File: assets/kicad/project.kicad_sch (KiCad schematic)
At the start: 22 parts, among them J1 Adafruit microSD, J2 EPD, J3 RTC, J4 Screw_Terminal_01x03

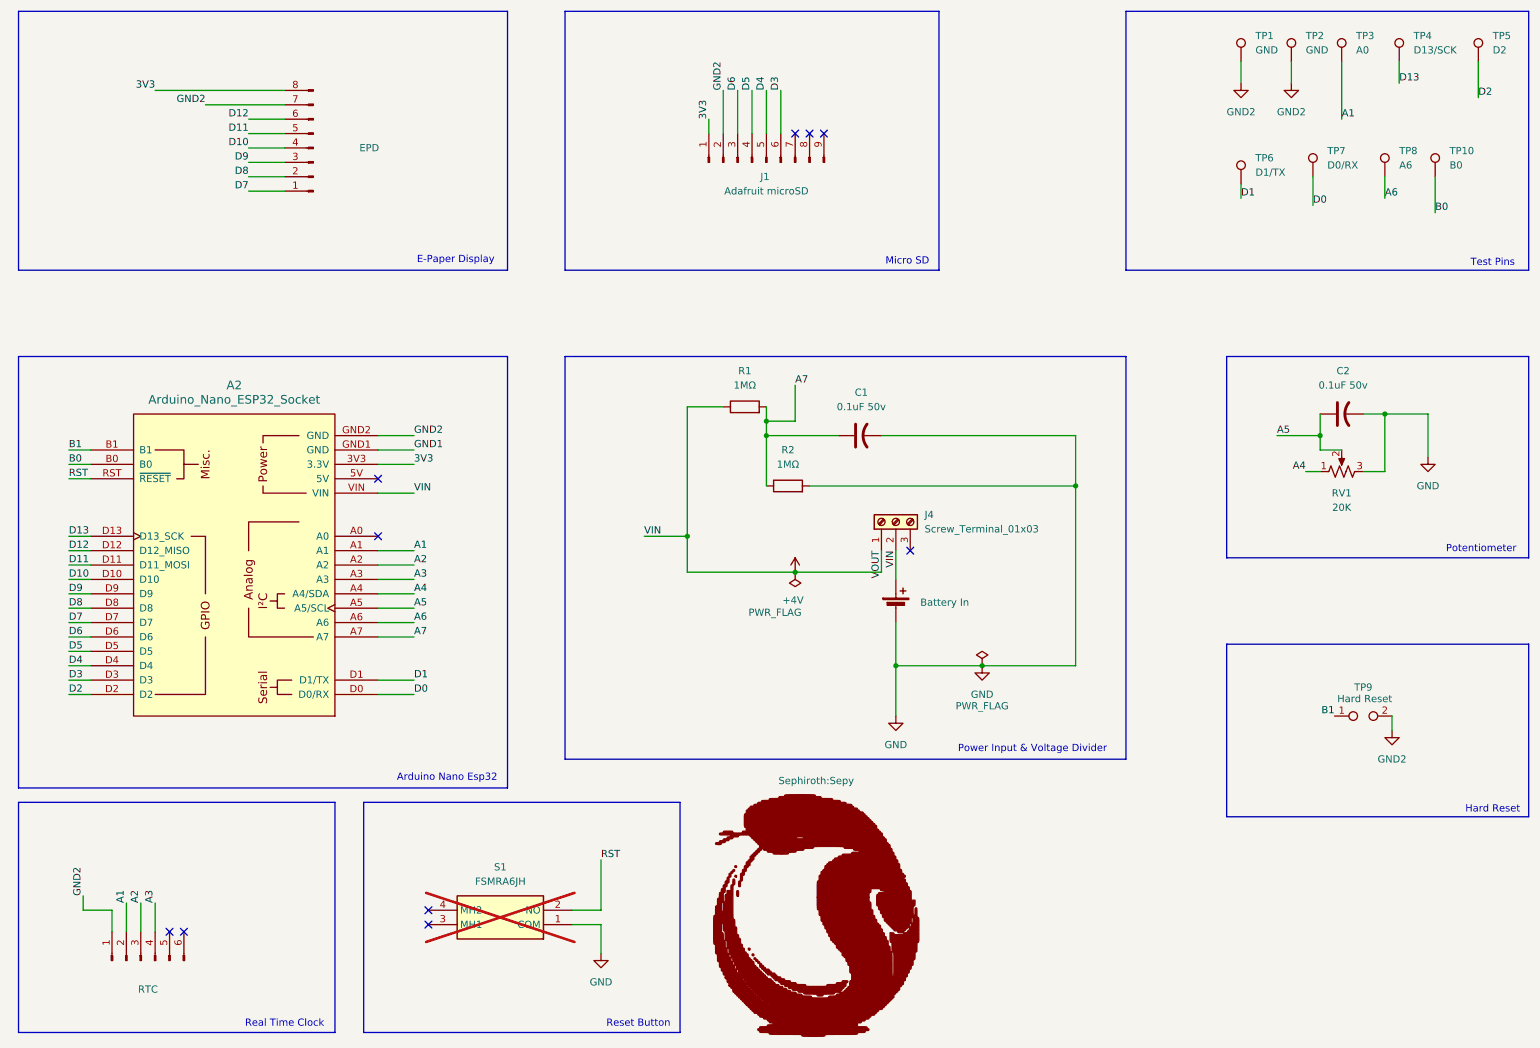
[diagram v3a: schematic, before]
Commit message: added support for 6 color e-display
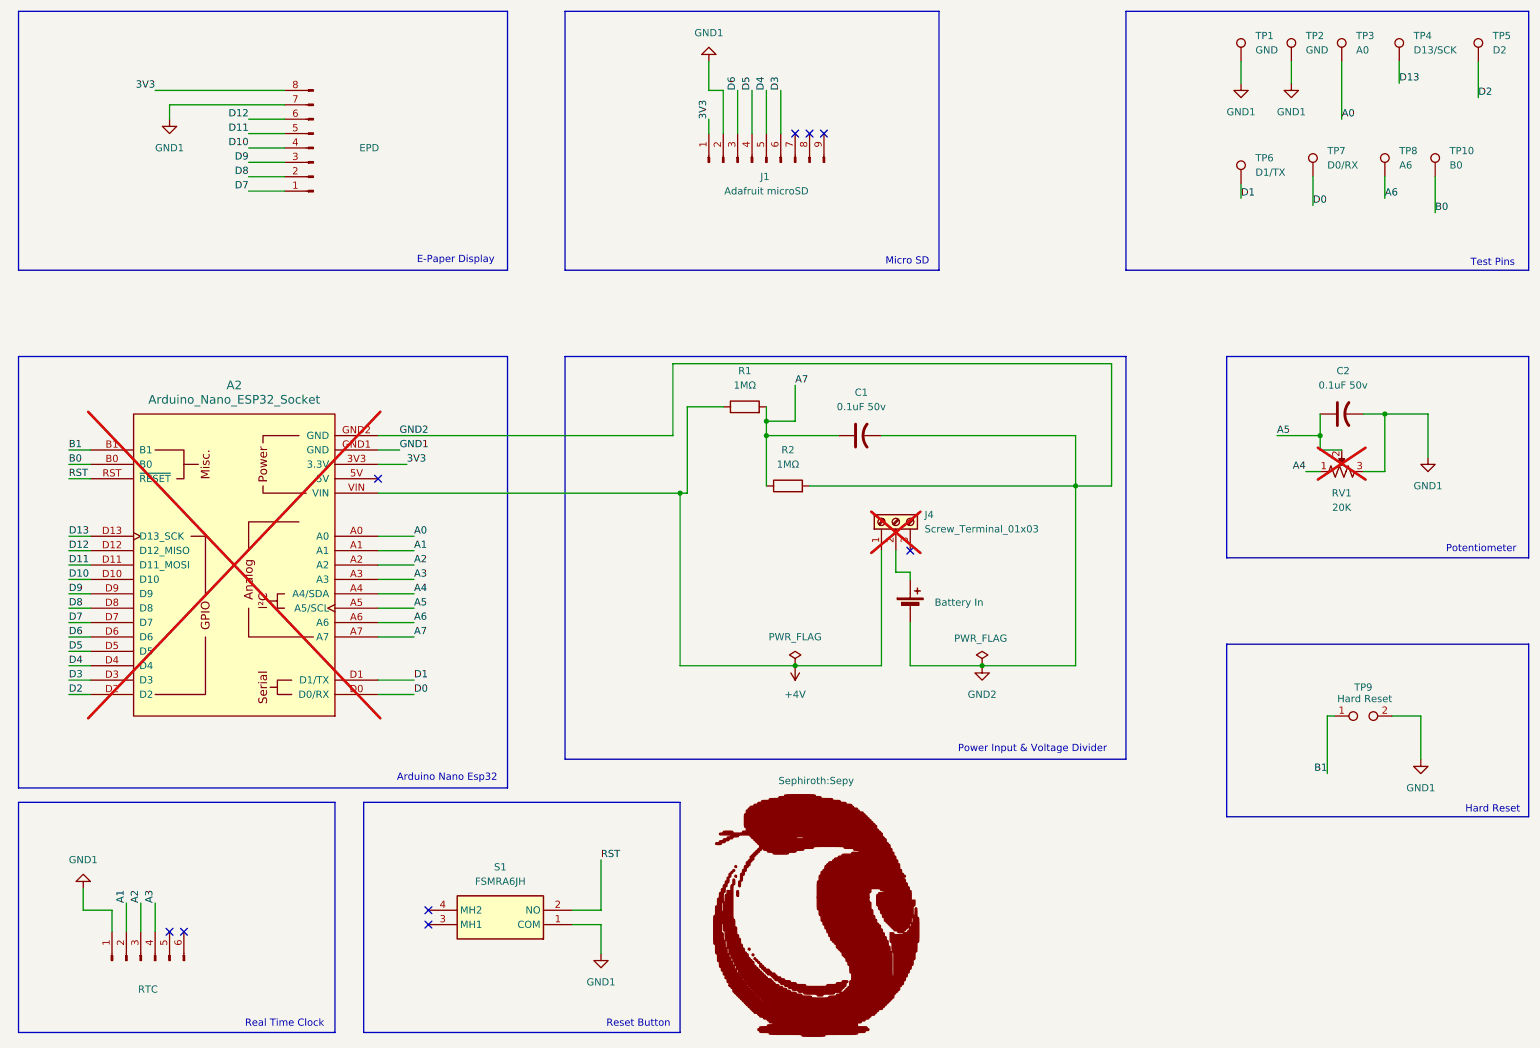
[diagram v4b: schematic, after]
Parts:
- A2, J4, RV1: now not fitted
- S1: now fitted
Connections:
- net +4V: no longer BT1.1 (+), J4.2 (Pin_2)
- net A1: no longer TP3.1
- net GND1: now also C2.2, J1.2 (Pin_2), J2.7 (Pin_7), J3.1 (Pin_1), RV1.3, S1.1 (COM), TP1.1, TP2.1, TP9.2
- net GND2: now also BT1.2 (-), C1.2, R2.2; no longer J1.2 (Pin_2), J2.7 (Pin_7), J3.1 (Pin_1), TP1.1, TP2.1, TP9.2
- net A0: now reaches A2.A0
- net A0: now also TP3.1
- removed net GND: BT1.2 (-), C1.2, C2.2, R2.2, RV1.3, S1.1 (COM)
- new net: BT1.1 (+), J4.2 (Pin_2)
- no-connect marks 10 -> 9

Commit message: pcb
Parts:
- A2: now left out of the parts list
- C1, C2, S1, TP1, TP10, TP2, TP3, TP4, TP6, TP7, TP8, TP9: now not fitted
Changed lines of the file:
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@@
 		(in_bom yes)
 		(on_board yes)
-		(dnp no)
+		(dnp yes)
 		(property "Reference" "TP9"
 			(at 252.73 134.62 0)
@@
 		(in_bom yes)
 		(on_board yes)
-		(dnp no)
+		(dnp yes)
 		(fields_autoplaced yes)
 		(property "Reference" "C1"
@@
 		(in_bom yes)
 		(on_board yes)
-		(dnp no)
+		(dnp yes)
 		(fields_autoplaced yes)
 		(property "Reference" "TP3"
@@
 		(in_bom yes)
 		(on_board yes)
-		(dnp no)
+		(dnp yes)
 		(fields_autoplaced yes)
 		(property "Reference" "S1"
@@
 		(in_bom yes)
 		(on_board yes)
-		(dnp no)
+		(dnp yes)
 		(fields_autoplaced yes)
 		(property "Reference" "TP8"
@@
 		(in_bom yes)
 		(on_board yes)
-		(dnp no)
+		(dnp yes)
 		(fields_autoplaced yes)
 		(property "Reference" "TP6"
@@
 		(in_bom yes)
 		(on_board yes)
-		(dnp no)
+		(dnp yes)
 		(fields_autoplaced yes)
 		(property "Reference" "TP4"
@@
 		(in_bom yes)
 		(on_board yes)
-		(dnp no)
+		(dnp yes)
 		(fields_autoplaced yes)
 		(property "Reference" "TP10"
@@
 		(in_bom yes)
 		(on_board yes)
-		(dnp no)
+		(dnp yes)
 		(fields_autoplaced yes)
 		(property "Reference" "C2"
@@
 		(in_bom yes)
 		(on_board yes)
-		(dnp no)
+		(dnp yes)
 		(property "Reference" "TP1"
 			(at 233.68 19.5579 0)
@@
 		(in_bom yes)
 		(on_board yes)
-		(dnp no)
+		(dnp yes)
 		(fields_autoplaced yes)
 		(property "Reference" "TP2"
@@
 		(unit 1)
 		(exclude_from_sim no)
-		(in_bom yes)
+		(in_bom no)
 		(on_board yes)
 		(dnp yes)
@@
 		(in_bom yes)
 		(on_board yes)
-		(dnp no)
+		(dnp yes)
 		(fields_autoplaced yes)
 		(property "Reference" "TP7"

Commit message: toggle RTC
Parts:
- removed TP6: D1/TX, Connector_Wire:SolderWire-0.5sqmm_1x01_D0.9mm_OD2.3mm, symbol Connector:TestPoint
- removed TP7: D0/RX, Connector_Wire:SolderWire-0.5sqmm_1x01_D0.9mm_OD2.3mm, symbol Connector:TestPoint
- removed TP8: A6, Connector_Wire:SolderWire-0.5sqmm_1x01_D0.9mm_OD2.3mm, symbol Connector:TestPoint
- BT1, R1, R2: now left out of the parts list
- C1, C2, J4, S1: now fitted; now left out of the parts list
- TP5: value D2 -> GND 2; now not fitted
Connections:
- net GND2: now also TP5.1
- net A6: no longer names the net of A2.A6
- net D0: no longer names the net of A2.D0 (D0/RX)
- net D1: no longer names the net of A2.D1 (D1/TX)
- net D2: no longer names the net of A2.D2
- net D2: no longer TP5.1
- no-connect marks 9 -> 13
